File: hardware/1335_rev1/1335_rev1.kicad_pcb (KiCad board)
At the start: 2 copper layers, 45 x 45 mm, 21 parts, among them J1 Screw_Terminal_01x05, J2 Screw_Terminal_01x06, U1 A1335

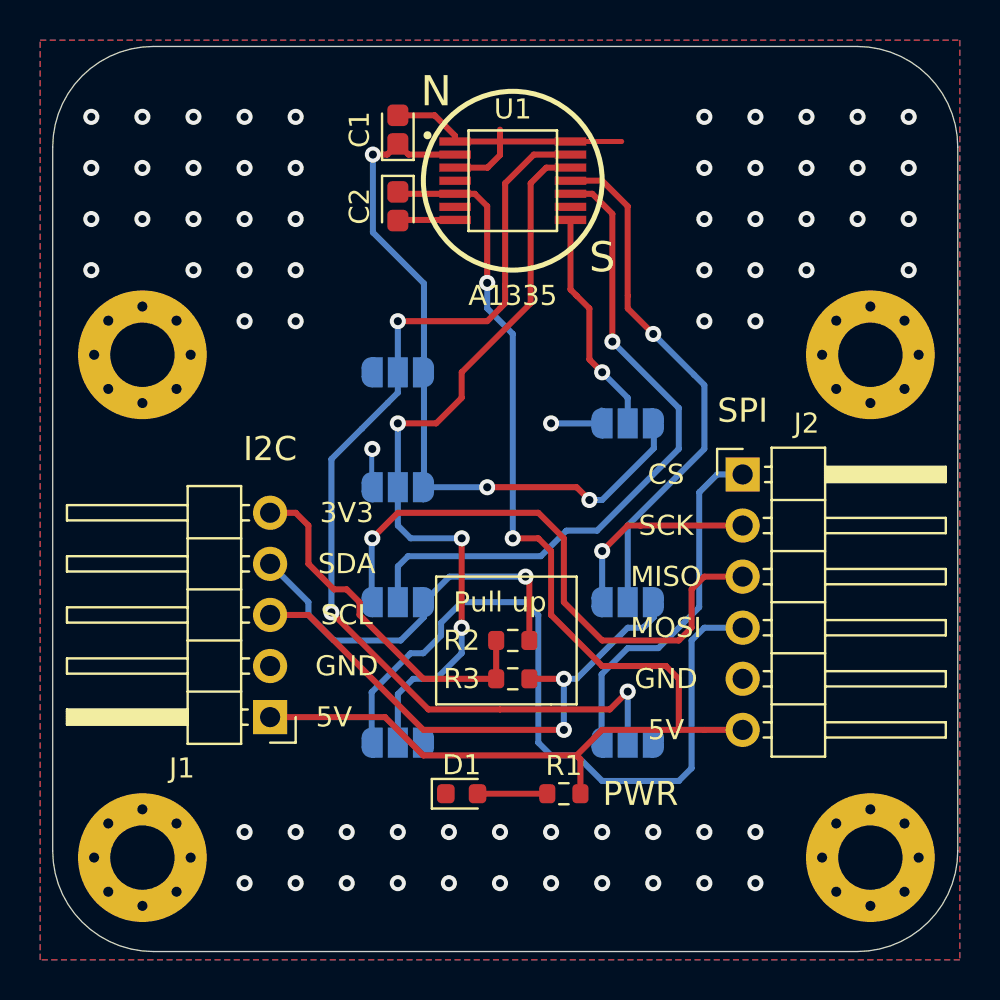
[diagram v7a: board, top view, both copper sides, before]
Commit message: Change position of mh
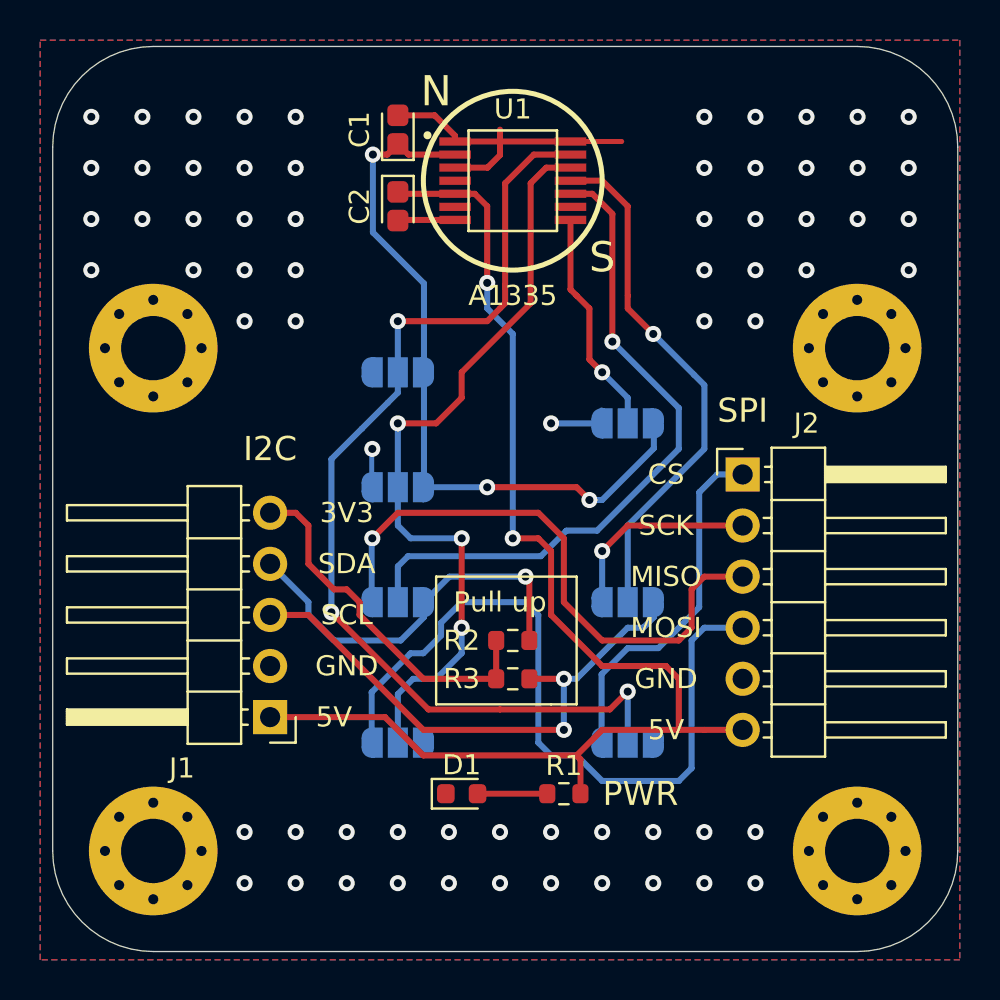
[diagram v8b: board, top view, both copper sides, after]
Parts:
- moved H2 0.73 mm to (160.0, 75.0)
- moved H4 0.73 mm to (160.0, 100.0)
- moved H1 0.63 mm to (125.0, 75.0)
- moved H3 0.63 mm to (125.0, 100.0)
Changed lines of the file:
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@@
   (general
     (thickness 1.6)
-    (drawings 58)
+    (drawings 67)
     (tracks 281)
     (zones 0)
@@
     (32 B.Adhes user hide)
     (33 F.Adhes user hide)
-    (34 B.Paste user)
-    (35 F.Paste user)
+    (34 B.Paste user hide)
+    (35 F.Paste user hide)
     (36 B.SilkS user)
     (37 F.SilkS user)
     (38 B.Mask user)
     (39 F.Mask user)
-    (40 Dwgs.User user hide)
+    (40 Dwgs.User user)
     (41 Cmts.User user hide)
     (42 Eco1.User user hide)
@@
     (44 Edge.Cuts user)
     (45 Margin user hide)
-    (46 B.CrtYd user hide)
-    (47 F.CrtYd user hide)
+    (46 B.CrtYd user)
+    (47 F.CrtYd user)
     (48 B.Fab user hide)
     (49 F.Fab user hide)
   )
   (setup
-    (last_trace_width 0.3)
+    (last_trace_width 0.25)
     (user_trace_width 0.3)
     (trace_clearance 0.2)
@@
     (visible_elements 7FFFFFFF)
     (pcbplotparams
-      (layerselection 0x010fc_ffffffff)
+      (layerselection 0x010f0_ffffffff)
       (usegerberextensions false)
       (usegerberattributes true)
@@
   )
   (module MountingHole:MountingHole_3.2mm_M3_Pad_Via (layer F.Cu)
-    (at 124.46 75.33)
+    (at 125 75)
     (descr "Mounting Hole 3.2mm, M3")
     (tags "mounting hole 3.2mm m3")
@@
   )
   (module MountingHole:MountingHole_3.2mm_M3_Pad_Via (layer F.Cu)
-    (at 160.655 75.33)
+    (at 160 75)
     (descr "Mounting Hole 3.2mm, M3")
     (tags "mounting hole 3.2mm m3")
@@
   )
   (module MountingHole:MountingHole_3.2mm_M3_Pad_Via (layer F.Cu)
-    (at 124.46 100.33)
+    (at 125 100)
     (descr "Mounting Hole 3.2mm, M3")
     (tags "mounting hole 3.2mm m3")
@@
   )
   (module MountingHole:MountingHole_3.2mm_M3_Pad_Via (layer F.Cu)
-    (at 160.655 100.33)
+    (at 160 100)
     (descr "Mounting Hole 3.2mm, M3")
     (tags "mounting hole 3.2mm m3")
@@
     )
   )
+  (dimension 25 (width 0.15) (layer Dwgs.User)
+    (gr_text "25.000 mm" (at 171.48 87.5 270) (layer Dwgs.User)
+      (effects (font (size 1 1) (thickness 0.15)))
+    )
+    (feature1 (pts (xy 160 100) (xy 170.766421 100)))
+    (feature2 (pts (xy 160 75) (xy 170.766421 75)))
+    (crossbar (pts (xy 170.18 75) (xy 170.18 100)))
+    (arrow1a (pts (xy 170.18 100) (xy 169.593579 98.873496)))
+    (arrow1b (pts (xy 170.18 100) (xy 170.766421 98.873496)))
+    (arrow2a (pts (xy 170.18 75) (xy 169.593579 76.126504)))
+    (arrow2b (pts (xy 170.18 75) (xy 170.766421 76.126504)))
+  )
+  (dimension 35 (width 0.15) (layer Dwgs.User)
+    (gr_text "35.000 mm" (at 142.5 110.52) (layer Dwgs.User)
+      (effects (font (size 1 1) (thickness 0.15)))
+    )
+    (feature1 (pts (xy 160 100) (xy 160 109.806421)))
+    (feature2 (pts (xy 125 100) (xy 125 109.806421)))
+    (crossbar (pts (xy 125 109.22) (xy 160 109.22)))
+    (arrow1a (pts (xy 160 109.22) (xy 158.873496 109.806421)))
+    (arrow1b (pts (xy 160 109.22) (xy 158.873496 108.633579)))
+    (arrow2a (pts (xy 125 109.22) (xy 126.126504 109.806421)))
+    (arrow2b (pts (xy 125 109.22) (xy 126.126504 108.633579)))
+  )
+  (dimension 25 (width 0.15) (layer Dwgs.User)
+    (gr_text "25.000 mm" (at 115.54 87.5 90) (layer Dwgs.User)
+      (effects (font (size 1 1) (thickness 0.15)))
+    )
+    (feature1 (pts (xy 125 75) (xy 116.253579 75)))
+    (feature2 (pts (xy 125 100) (xy 116.253579 100)))
+    (crossbar (pts (xy 116.84 100) (xy 116.84 75)))
+    (arrow1a (pts (xy 116.84 75) (xy 117.426421 76.126504)))
+    (arrow1b (pts (xy 116.84 75) (xy 116.253579 76.126504)))
+    (arrow2a (pts (xy 116.84 100) (xy 117.426421 98.873496)))
+    (arrow2b (pts (xy 116.84 100) (xy 116.253579 98.873496)))
+  )
+  (dimension 5 (width 0.15) (layer Dwgs.User)
+    (gr_text "5.000 mm" (at 171.48 102.5 270) (layer Dwgs.User)
+      (effects (font (size 1 1) (thickness 0.15)))
+    )
+    (feature1 (pts (xy 160 105) (xy 170.766421 105)))
+    (feature2 (pts (xy 160 100) (xy 170.766421 100)))
+    (crossbar (pts (xy 170.18 100) (xy 170.18 105)))
+    (arrow1a (pts (xy 170.18 105) (xy 169.593579 103.873496)))
+    (arrow1b (pts (xy 170.18 105) (xy 170.766421 103.873496)))
+    (arrow2a (pts (xy 170.18 100) (xy 169.593579 101.126504)))
+    (arrow2b (pts (xy 170.18 100) (xy 170.766421 101.126504)))
+  )
+  (dimension 5 (width 0.15) (layer Dwgs.User)
+    (gr_text "5.000 mm" (at 162.5 110.52) (layer Dwgs.User)
+      (effects (font (size 1 1) (thickness 0.15)))
+    )
+    (feature1 (pts (xy 165 100) (xy 165 109.806421)))
+    (feature2 (pts (xy 160 100) (xy 160 109.806421)))
+    (crossbar (pts (xy 160 109.22) (xy 165 109.22)))
+    (arrow1a (pts (xy 165 109.22) (xy 163.873496 109.806421)))
+    (arrow1b (pts (xy 165 109.22) (xy 163.873496 108.633579)))
+    (arrow2a (pts (xy 160 109.22) (xy 161.126504 109.806421)))
+    (arrow2b (pts (xy 160 109.22) (xy 161.126504 108.633579)))
+  )
+  (dimension 5 (width 0.15) (layer Dwgs.User)
+    (gr_text "5.000 mm" (at 115.54 102.5 90) (layer Dwgs.User)
+      (effects (font (size 1 1) (thickness 0.15)))
+    )
+    (feature1 (pts (xy 125 100) (xy 116.253579 100)))
+    (feature2 (pts (xy 125 105) (xy 116.253579 105)))
+    (crossbar (pts (xy 116.84 105) (xy 116.84 100)))
+    (arrow1a (pts (xy 116.84 100) (xy 117.426421 101.126504)))
+    (arrow1b (pts (xy 116.84 100) (xy 116.253579 101.126504)))
+    (arrow2a (pts (xy 116.84 105) (xy 117.426421 103.873496)))
+    (arrow2b (pts (xy 116.84 105) (xy 116.253579 103.873496)))
+  )
+  (dimension 5 (width 0.15) (layer Dwgs.User)
+    (gr_text "5.000 mm" (at 122.5 110.52) (layer Dwgs.User)
+      (effects (font (size 1 1) (thickness 0.15)))
+    )
+    (feature1 (pts (xy 120 100) (xy 120 109.806421)))
+    (feature2 (pts (xy 125 100) (xy 125 109.806421)))
+    (crossbar (pts (xy 125 109.22) (xy 120 109.22)))
+    (arrow1a (pts (xy 120 109.22) (xy 121.126504 108.633579)))
+    (arrow1b (pts (xy 120 109.22) (xy 121.126504 109.806421)))
+    (arrow2a (pts (xy 125 109.22) (xy 123.873496 108.633579)))
+    (arrow2b (pts (xy 125 109.22) (xy 123.873496 109.806421)))
+  )
+  (dimension 4.445041 (width 0.15) (layer Dwgs.User)
+    (gr_text "4.445 mm" (at 122.334281 52.678931 -0.2449073522) (layer Dwgs.User)
+      (effects (font (size 1 1) (thickness 0.15)))
+    )
+    (feature1 (pts (xy 120.015 75.311) (xy 120.10873 53.383004)))
+    (feature2 (pts (xy 124.46 75.33) (xy 124.55373 53.402004)))
+    (crossbar (pts (xy 124.551224 53.988419) (xy 120.106224 53.969419)))
+    (arrow1a (pts (xy 120.106224 53.969419) (xy 121.235224 53.387819)))
+    (arrow1b (pts (xy 120.106224 53.969419) (xy 121.230211 54.56065)))
+    (arrow2a (pts (xy 124.551224 53.988419) (xy 123.427237 53.397188)))
+    (arrow2b (pts (xy 124.551224 53.988419) (xy 123.422224 54.570019)))
+  )
+  (dimension 36.195 (width 0.15) (layer Dwgs.User)
+    (gr_text "36.195 mm" (at 142.5575 52.675) (layer Dwgs.User)
+      (effects (font (size 1 1) (thickness 0.15)))
+    )
+    (feature1 (pts (xy 124.46 75.33) (xy 124.46 53.388579)))
+    (feature2 (pts (xy 160.655 75.33) (xy 160.655 53.388579)))
+    (crossbar (pts (xy 160.655 53.975) (xy 124.46 53.975)))
+    (arrow1a (pts (xy 124.46 53.975) (xy 125.586504 53.388579)))
+    (arrow1b (pts (xy 124.46 53.975) (xy 125.586504 54.561421)))
+    (arrow2a (pts (xy 160.655 53.975) (xy 159.528496 53.388579)))
+    (arrow2b (pts (xy 160.655 53.975) (xy 159.528496 54.561421)))
+  )
   (gr_text "Rev 2.0" (at 142.875 66.675) (layer B.SilkS)
